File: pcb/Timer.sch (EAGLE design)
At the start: 42 parts, among them Q1 8MHz, U1 ATTINY24SSU, U2 SCT2024CSOG, U3 SCT2024CSOG, U4 LD117AS33TR

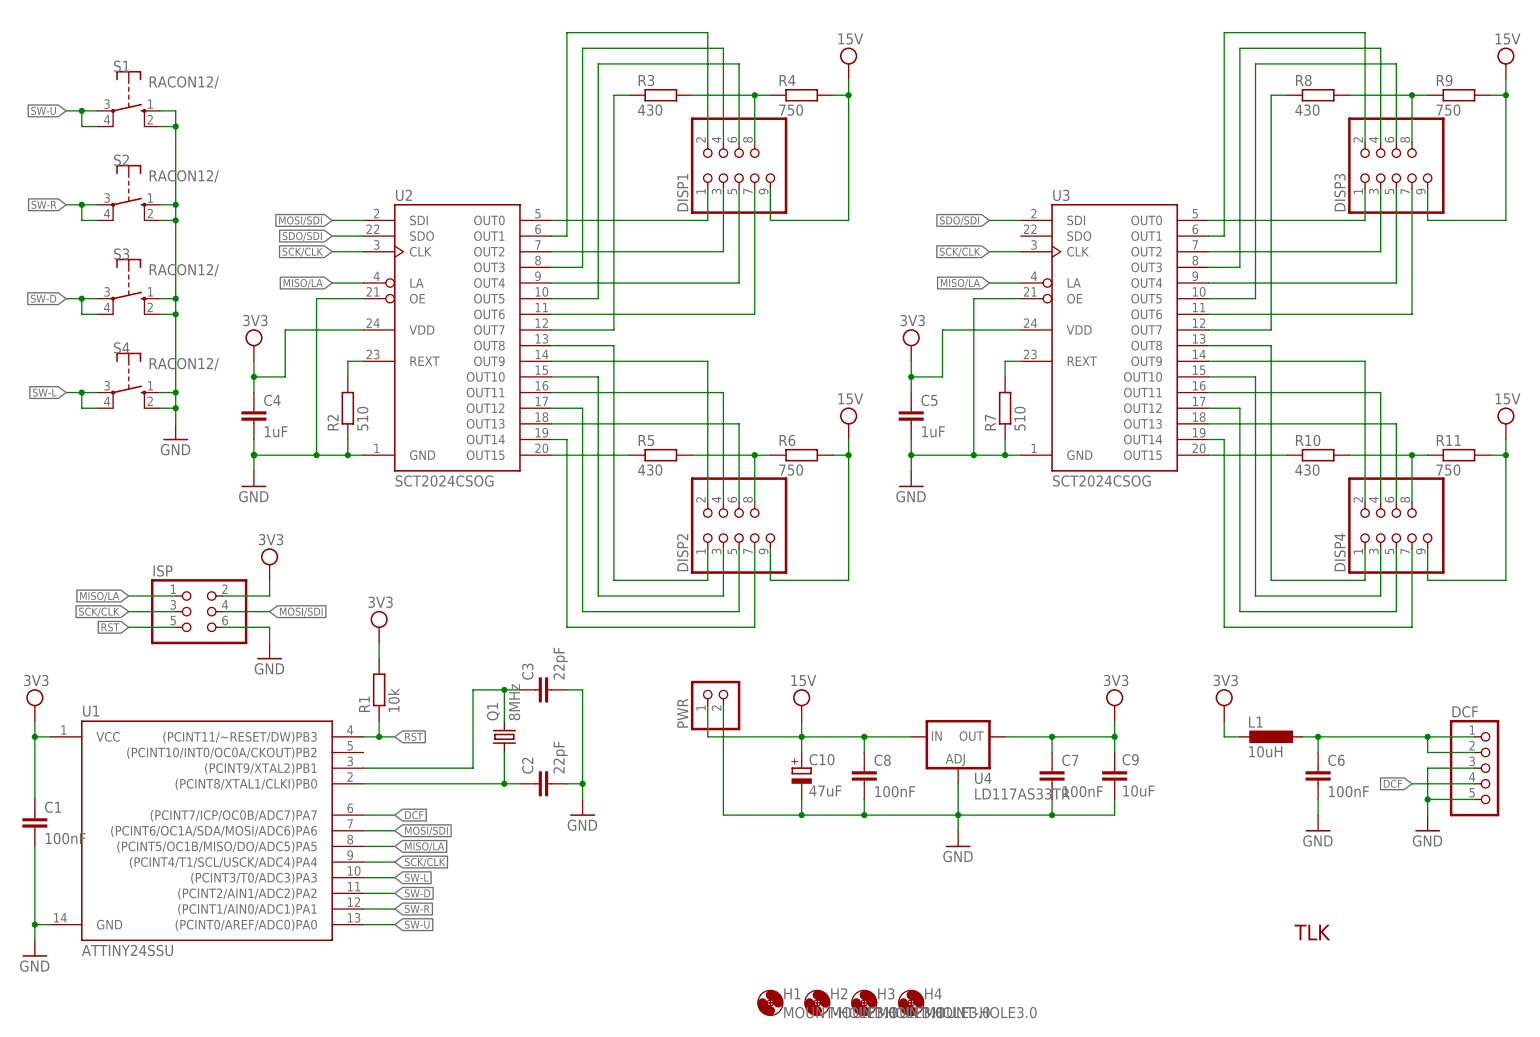
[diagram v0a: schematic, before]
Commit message: Add Extension connector, move some traces
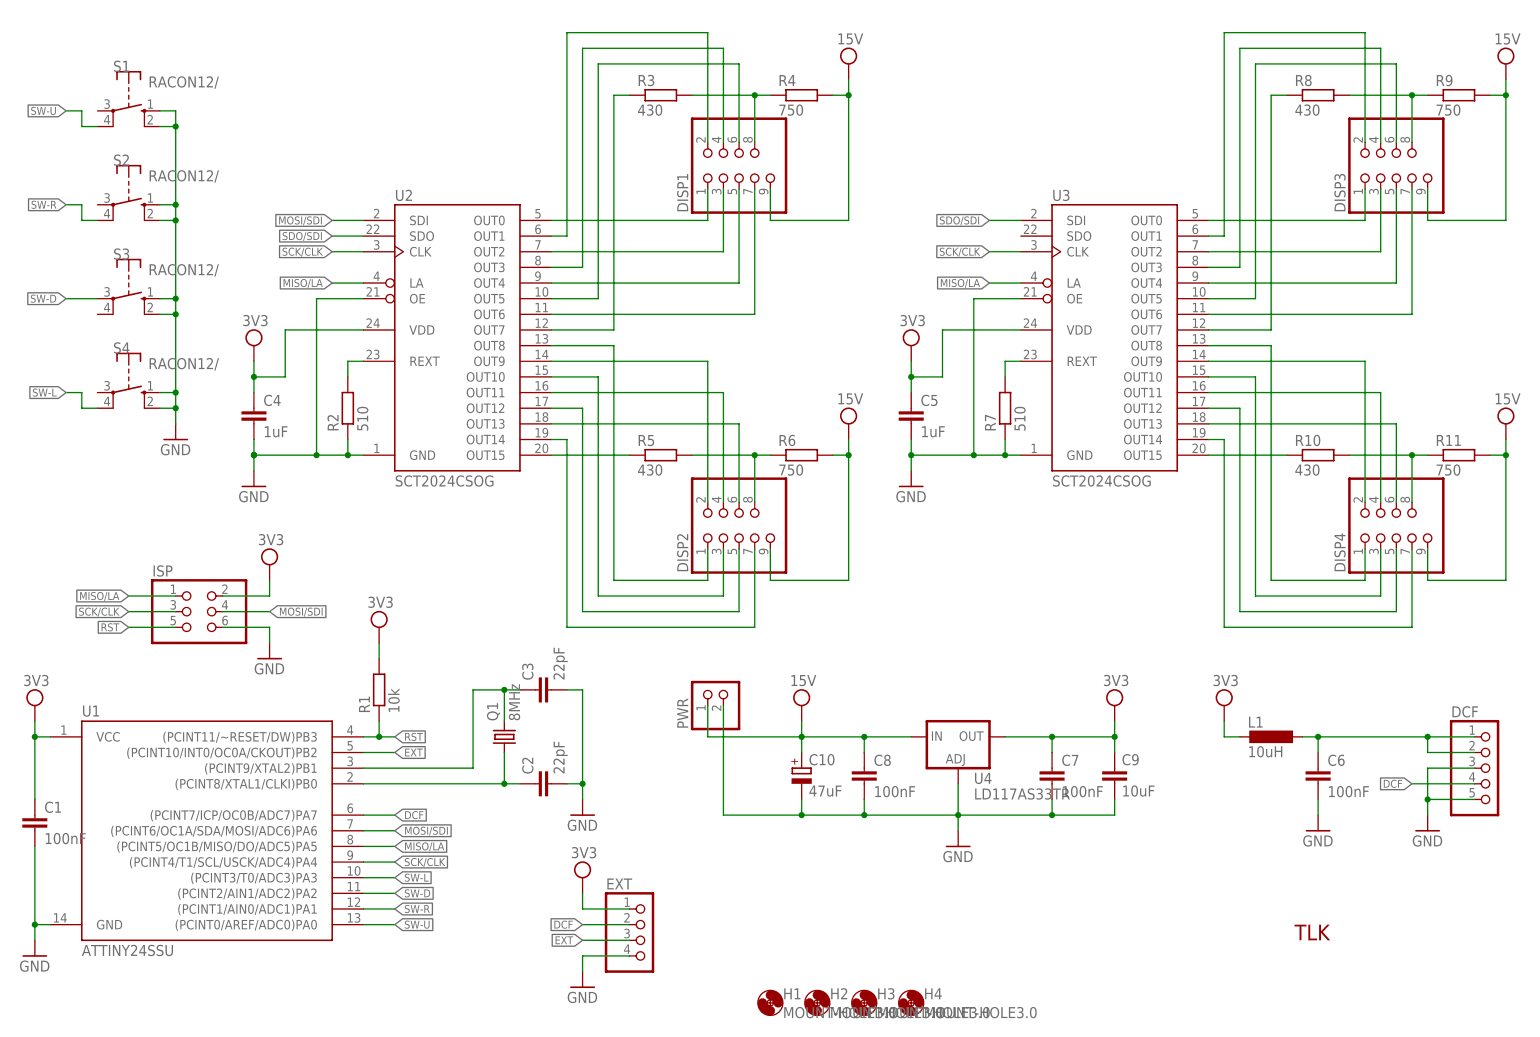
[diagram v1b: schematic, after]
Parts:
- added EXT: (no value), pinhead-2:PINHD-1X4/90
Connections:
- new net EXT: EXT.3, U1.(PCINT10/INT0/OC0A/CKOUT)PB2
- net DCF: now also EXT.2
- net GND: now also EXT.4
- net SW-D: no longer S3.P@1
- net SW-L: no longer S4.P
- net SW-R: no longer S2.P
- net SW-U: no longer S1.P
- net VCC: now also EXT.1
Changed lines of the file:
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@@
 <part name="DISP3" library=".MW" deviceset="DISP-CON" device="" package3d_urn="urn:adsk.eagle:package:22471/2"/>
 <part name="DISP4" library=".MW" deviceset="DISP-CON" device="" package3d_urn="urn:adsk.eagle:package:22471/2"/>
+<part name="EXT" library="pinhead-2" deviceset="PINHD-1X4" device="/90" package3d_urn="urn:adsk.eagle:package:22404/2"/>
+<part name="SUPPLY13" library="supply2" library_urn="urn:adsk.eagle:library:372" deviceset="VCC" device="" value="3V3"/>
+<part name="GND10" library="supply1" library_urn="urn:adsk.eagle:library:371" deviceset="GND" device=""/>
 </parts>
 <sheets>
@@
 <attribute name="NAME" x="225.425" y="80.01" size="1.778" layer="95" rot="R90"/>
 <attribute name="VALUE" x="243.84" y="80.01" size="1.778" layer="96" rot="R90"/>
+</instance>
+<instance part="EXT" gate="A" x="111.76" y="20.32" smashed="yes">
+<attribute name="NAME" x="105.41" y="28.575" size="1.778" layer="95"/>
+<attribute name="VALUE" x="105.41" y="12.7" size="1.778" layer="96"/>
+</instance>
+<instance part="SUPPLY13" gate="G$1" x="101.6" y="30.48" smashed="yes">
+<attribute name="VALUE" x="99.695" y="33.655" size="1.778" layer="96"/>
+</instance>
+<instance part="GND10" gate="1" x="101.6" y="12.7" smashed="yes">
+<attribute name="VALUE" x="99.06" y="10.16" size="1.778" layer="96"/>
 </instance>
 </instances>
@@
 <pinref part="SUPPLY12" gate="G$1" pin="VCC"/>
 <pinref part="ISP" gate="A" pin="2"/>
+</segment>
+<segment>
+<pinref part="EXT" gate="A" pin="1"/>
+<pinref part="SUPPLY13" gate="G$1" pin="VCC"/>
+<wire x1="109.22" y1="25.4" x2="101.6" y2="25.4" width="0.1524" layer="91"/>
+<wire x1="101.6" y1="25.4" x2="101.6" y2="27.94" width="0.1524" layer="91"/>
 </segment>
 </net>
@@
 <pinref part="ISP" gate="A" pin="6"/>
 </segment>
+<segment>
+<pinref part="EXT" gate="A" pin="4"/>
+<pinref part="GND10" gate="1" pin="GND"/>
+<wire x1="109.22" y1="17.78" x2="101.6" y2="17.78" width="0.1524" layer="91"/>
+<wire x1="101.6" y1="17.78" x2="101.6" y2="15.24" width="0.1524" layer="91"/>
+</segment>
 </net>
 <net name="MOSI/SDI" class="0">
@@
 <wire x1="66.04" y1="40.64" x2="71.12" y2="40.64" width="0.1524" layer="91"/>
 <label x="71.12" y="40.64" size="1.27" layer="95" xref="yes"/>
+</segment>
+<segment>
+<pinref part="EXT" gate="A" pin="2"/>
+<wire x1="109.22" y1="22.86" x2="101.6" y2="22.86" width="0.1524" layer="91"/>
+<label x="101.6" y="22.86" size="1.27" layer="95" rot="R180" xref="yes"/>
 </segment>
 </net>
@@
 <net name="SW-U" class="0">
 <segment>
-<wire x1="22.86" y1="154.94" x2="20.32" y2="154.94" width="0.1524" layer="91"/>
 <wire x1="20.32" y1="154.94" x2="20.32" y2="152.4" width="0.1524" layer="91"/>
 <wire x1="20.32" y1="152.4" x2="22.86" y2="152.4" width="0.1524" layer="91"/>
 <wire x1="20.32" y1="154.94" x2="17.78" y2="154.94" width="0.1524" layer="91"/>
-<junction x="20.32" y="154.94"/>
 <label x="17.78" y="154.94" size="1.27" layer="95" rot="R180" xref="yes"/>
-<pinref part="S1" gate="1" pin="P"/>
 <pinref part="S1" gate="1" pin="P@1"/>
 </segment>
@@
 <net name="SW-L" class="0">
 <segment>
-<wire x1="22.86" y1="109.22" x2="20.32" y2="109.22" width="0.1524" layer="91"/>
 <wire x1="20.32" y1="109.22" x2="20.32" y2="106.68" width="0.1524" layer="91"/>
 <wire x1="20.32" y1="106.68" x2="22.86" y2="106.68" width="0.1524" layer="91"/>
 <wire x1="20.32" y1="109.22" x2="17.78" y2="109.22" width="0.1524" layer="91"/>
-<junction x="20.32" y="109.22"/>
 <label x="17.78" y="109.22" size="1.27" layer="95" rot="R180" xref="yes"/>
-<pinref part="S4" gate="1" pin="P"/>
 <pinref part="S4" gate="1" pin="P@1"/>
 </segment>
@@
 <net name="SW-R" class="0">
 <segment>
-<wire x1="22.86" y1="139.7" x2="20.32" y2="139.7" width="0.1524" layer="91"/>
 <wire x1="20.32" y1="139.7" x2="20.32" y2="137.16" width="0.1524" layer="91"/>
 <wire x1="20.32" y1="137.16" x2="22.86" y2="137.16" width="0.1524" layer="91"/>
 <wire x1="20.32" y1="139.7" x2="17.78" y2="139.7" width="0.1524" layer="91"/>
-<junction x="20.32" y="139.7"/>
 <label x="17.78" y="139.7" size="1.27" layer="95" rot="R180" xref="yes"/>
-<pinref part="S2" gate="1" pin="P"/>
 <pinref part="S2" gate="1" pin="P@1"/>
 </segment>
@@
 <net name="SW-D" class="0">
 <segment>
-<wire x1="22.86" y1="121.92" x2="20.32" y2="121.92" width="0.1524" layer="91"/>
-<wire x1="20.32" y1="121.92" x2="20.32" y2="124.46" width="0.1524" layer="91"/>
-<wire x1="20.32" y1="124.46" x2="22.86" y2="124.46" width="0.1524" layer="91"/>
-<wire x1="20.32" y1="124.46" x2="17.78" y2="124.46" width="0.1524" layer="91"/>
-<junction x="20.32" y="124.46"/>
+<wire x1="22.86" y1="124.46" x2="17.78" y2="124.46" width="0.1524" layer="91"/>
 <label x="17.78" y="124.46" size="1.27" layer="95" rot="R180" xref="yes"/>
 <pinref part="S3" gate="1" pin="P"/>
-<pinref part="S3" gate="1" pin="P@1"/>
 </segment>
 <segment>
@@
 </segment>
 </net>
+<net name="EXT" class="0">
+<segment>
+<pinref part="U1" gate="A" pin="(PCINT10/INT0/OC0A/CKOUT)PB2"/>
+<wire x1="66.04" y1="50.8" x2="71.12" y2="50.8" width="0.1524" layer="91"/>
+<label x="71.12" y="50.8" size="1.27" layer="95" xref="yes"/>
+</segment>
+<segment>
+<pinref part="EXT" gate="A" pin="3"/>
+<wire x1="109.22" y1="20.32" x2="101.6" y2="20.32" width="0.1524" layer="91"/>
+<label x="101.6" y="20.32" size="1.27" layer="95" rot="R180" xref="yes"/>
+</segment>
+</net>

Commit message: Update footprints and silkscreen
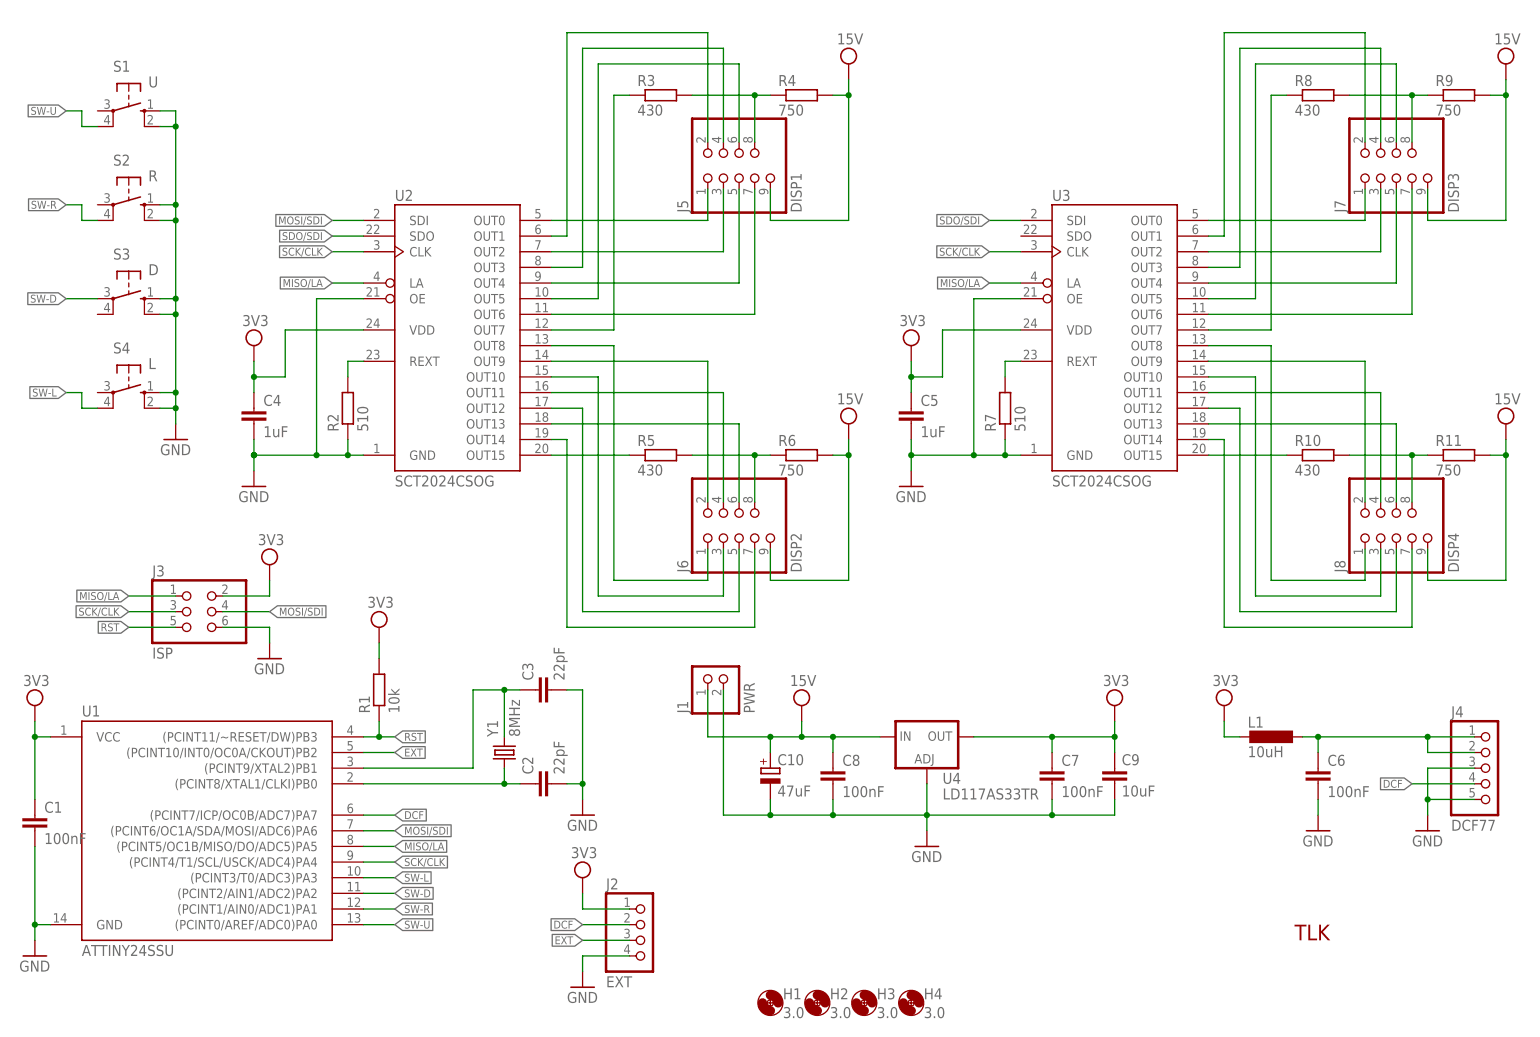
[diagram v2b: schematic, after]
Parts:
- removed DCF: (no value), pinhead-2:PINHD-1X5/90
- removed DISP1, DISP2, DISP3, DISP4: (no value), .MW:DISP-CON
- removed EXT: (no value), pinhead-2:PINHD-1X4/90
- removed ISP: (no value), pinhead-2:PINHD-2X3/90
- removed PWR: (no value), pinhead-2:PINHD-1X2/90
- removed Q1: 8MHz, crystal:CRYSTALHC49UP
- added J1: PWR, .pinhead:PINHD-1X2/90
- added J2: EXT, .pinhead:PINHD-1X4/90
- added J3: ISP, .pinhead:PINHD-2X3/90
- added J4: DCF77, .pinhead:PINHD-1X5/90
- added J5: DISP1, .pinhead:PINHD-2X4/5/90
- added J6: DISP2, .pinhead:PINHD-2X4/5/90
- added J7: DISP3, .pinhead:PINHD-2X4/5/90
- added J8: DISP4, .pinhead:PINHD-2X4/5/90
- added Y1: 8MHz, .crystal:CRYSTALHC49UP
- C1, C2, C3, C4, C5, C6, C7, C8, C9: device rcl:C-EUC0805 -> .rcl:C-EUC0805
- C10: device rcl:CPOL-EUE2.5-5 -> .rcl:CPOL-EUE2.5
- H1, H2, H3, H4: value MOUNT-HOLE3.0 -> 3.0
- L1: device .MW:L-EUL0805 -> .rcl:L-EUL0805
- R1, R2, R7: device rcl:R-EU_R0805 -> .rcl:R-EUR0805
- R10, R11, R3, R4, R5, R6, R8, R9: device rcl:R-EU_R1206 -> .rcl:R-EUR1206
- S1: value RACON12/ -> U; device switch-misc:RACON12/ -> .switch:TACT
- S2: value RACON12/ -> R; device switch-misc:RACON12/ -> .switch:TACT
- S3: value RACON12/ -> D; device switch-misc:RACON12/ -> .switch:TACT
- S4: value RACON12/ -> L; device switch-misc:RACON12/ -> .switch:TACT
- U1: device .MW:ATTINY24SSU -> .atmel:ATTINY24SSU
- U2, U3: device .MW:SCT2024CSOG -> .starchips:SCT2024CSOG
- U4: device v-reg:LD117AS33TR -> .v-reg:LD117AS33TR
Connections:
- net DCF: now also J2.2, J4.4; no longer DCF.4, EXT.2
- net EXT: now also J2.3; no longer EXT.3
- net GND: now also J1.2, J2.4, J3.6, J4.3, J4.5, S1.S1, S2.S1, S3.S1, S4.S1; no longer DCF.3, DCF.5, EXT.4, ISP.6, PWR.2, S1.S@1, S2.S@1, S3.S@1, S4.S@1
- net MISO/LA: now also J3.1; no longer ISP.1
- net MOSI/SDI: now also J3.4; no longer ISP.4
- net N$1: now also Y1.2; no longer Q1.2
- net N$10: now also J5.8; no longer DISP1.8
- net N$11: now also J5.7; no longer DISP1.7
- net N$13: now also J6.2; no longer DISP2.2
- net N$14: now also J7.1; no longer DISP3.1
- net N$15: now also J7.3; no longer DISP3.3
- net N$16: now also J7.5; no longer DISP3.5
- net N$17: now also J7.7; no longer DISP3.7
- net N$18: now also J7.2; no longer DISP3.2
- net N$19: now also J7.4; no longer DISP3.4
- net N$2: now also Y1.1; no longer Q1.1
- net N$20: now also J7.6; no longer DISP3.6
- net N$21: now also J7.8; no longer DISP3.8
- net N$22: now also J6.4; no longer DISP2.4
- net N$24: now also J8.2; no longer DISP4.2
- net N$25: now also J8.4; no longer DISP4.4
- net N$26: now also J8.6; no longer DISP4.6
- net N$28: now also J8.8; no longer DISP4.8
- net N$3: now also J4.1, J4.2; no longer DCF.1, DCF.2
- net N$30: now also J8.1; no longer DISP4.1
- net N$31: now also J8.3; no longer DISP4.3
- net N$32: now also J8.5; no longer DISP4.5
- net N$33: now also J6.6; no longer DISP2.6
- net N$34: now also J6.8; no longer DISP2.8
- net N$35: now also J6.7; no longer DISP2.7
- net N$36: now also J6.5; no longer DISP2.5
- net N$39: now also J6.3; no longer DISP2.3
- net N$4: now also J5.1; no longer DISP1.1
- net N$40: now also J6.1; no longer DISP2.1
- net N$42: now also J8.7; no longer DISP4.7
- net N$5: now also J5.2; no longer DISP1.2
- net N$6: now also J5.3; no longer DISP1.3
- net N$7: now also J5.4; no longer DISP1.4
- net N$8: now also J5.5; no longer DISP1.5
- net N$9: now also J5.6; no longer DISP1.6
- net RST: now also J3.5; no longer ISP.5
- net SCK/CLK: now also J3.3; no longer ISP.3
- net SW-L: now also S4.P1; no longer S4.P@1
- net SW-R: now also S2.P1; no longer S2.P@1
- net SW-U: now also S1.P1; no longer S1.P@1
- net VCC: now also J2.1, J3.2; no longer EXT.1, ISP.2
- net VDD: now also J1.1, J5.9, J6.9, J7.9, J8.9; no longer DISP1.9, DISP2.9, DISP3.9, DISP4.9, PWR.1
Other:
- moved on the sheet: C10, C8, U4
